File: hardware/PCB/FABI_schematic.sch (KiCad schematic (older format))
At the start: 45 parts, among them J1 Cliff_68125, J10 Conn_01x03_Male, J11 dispaly_connector_91601-304LF, J11_GND1 Conn_01x01_Male, J11_VDD1 Conn_01x01_Male, J11_data1 Conn_01x01_Male, J2 Cliff_68125, J3 Cliff_68125, J4 Cliff_68125, J5 Cliff_68125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

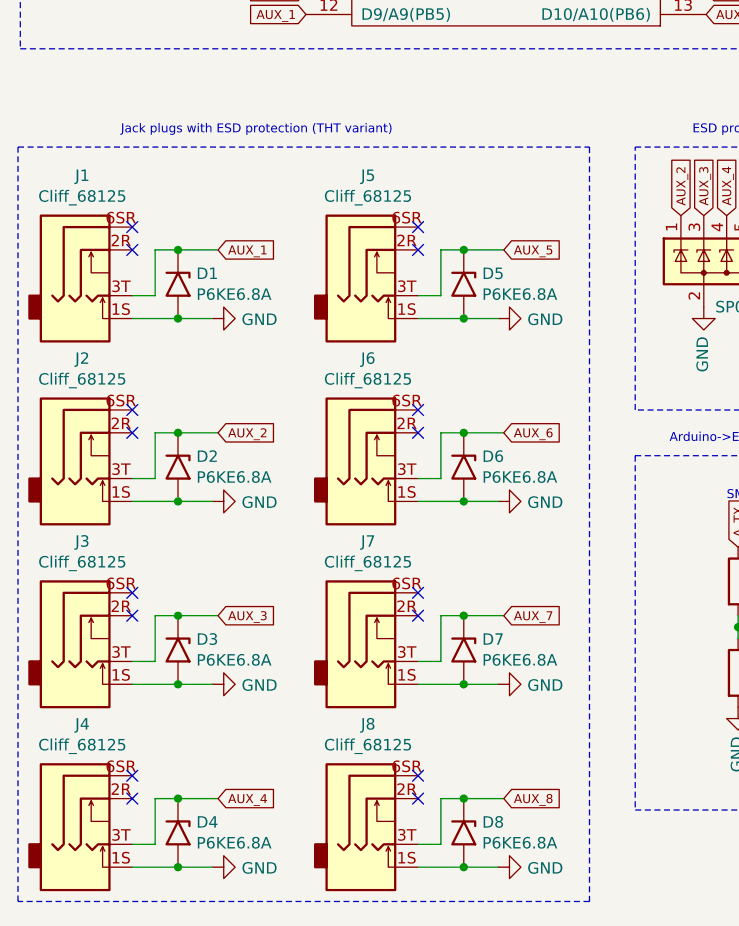
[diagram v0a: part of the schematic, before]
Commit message: JackPlugs in Schematic changed
Signed-off-by: fussthalerandreas <fussthaler.andreas1997@gmail.com>
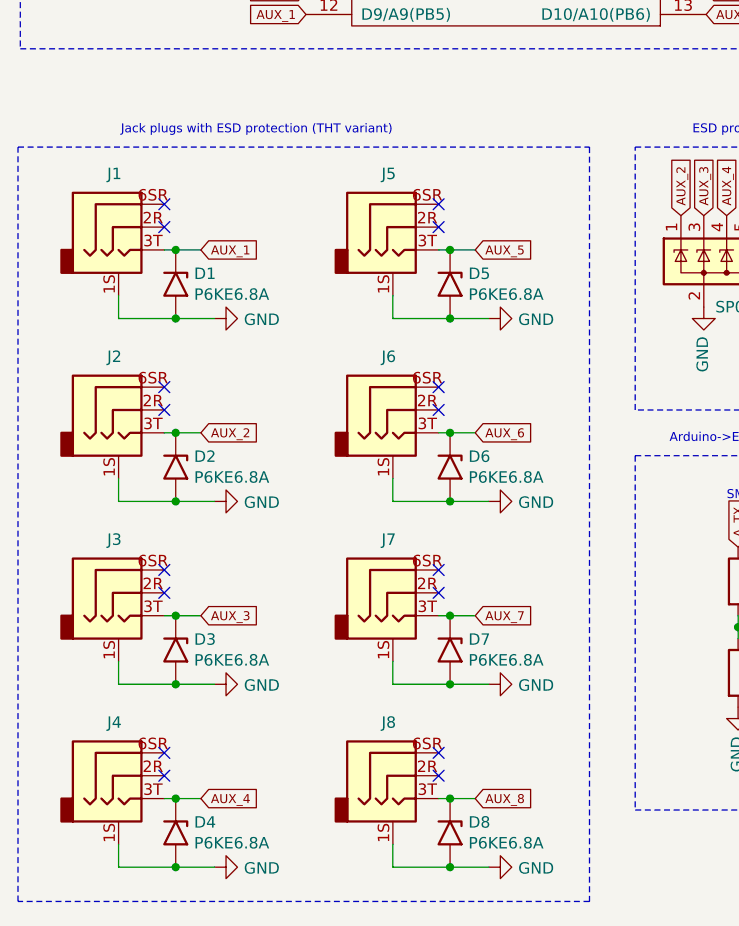
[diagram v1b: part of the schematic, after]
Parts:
- removed J1, J2, J3, J4, J5, J6, J7, J8: Cliff_68125, SamacSys_Parts:FC68125, symbol Connector:Cliff_68125
- added J1, J2, J3, J4, J5, J6, J7, J8: AudioJack3_Ground, SamacSys_Parts:FC68125, symbol FABI_customLib:AudioJack3_Ground
- J11: RS (none) -> https://at.rs-online.com/web/p/leiterplatten-buchsen/673740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
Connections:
- net AUX_1: now also J1.3T
- net AUX_2: now also J2.3T
- net AUX_3: now also J3.3T
- net AUX_4: now also J4.3T
- net AUX_5: now also J5.3T
- net AUX_6: now also J6.3T
- net AUX_7: now also J7.3T
- net AUX_8: now also J8.3T
- net GND: now also J1.1S, J2.1S, J3.1S, J4.1S, J5.1S, J6.1S, J7.1S, J8.1S

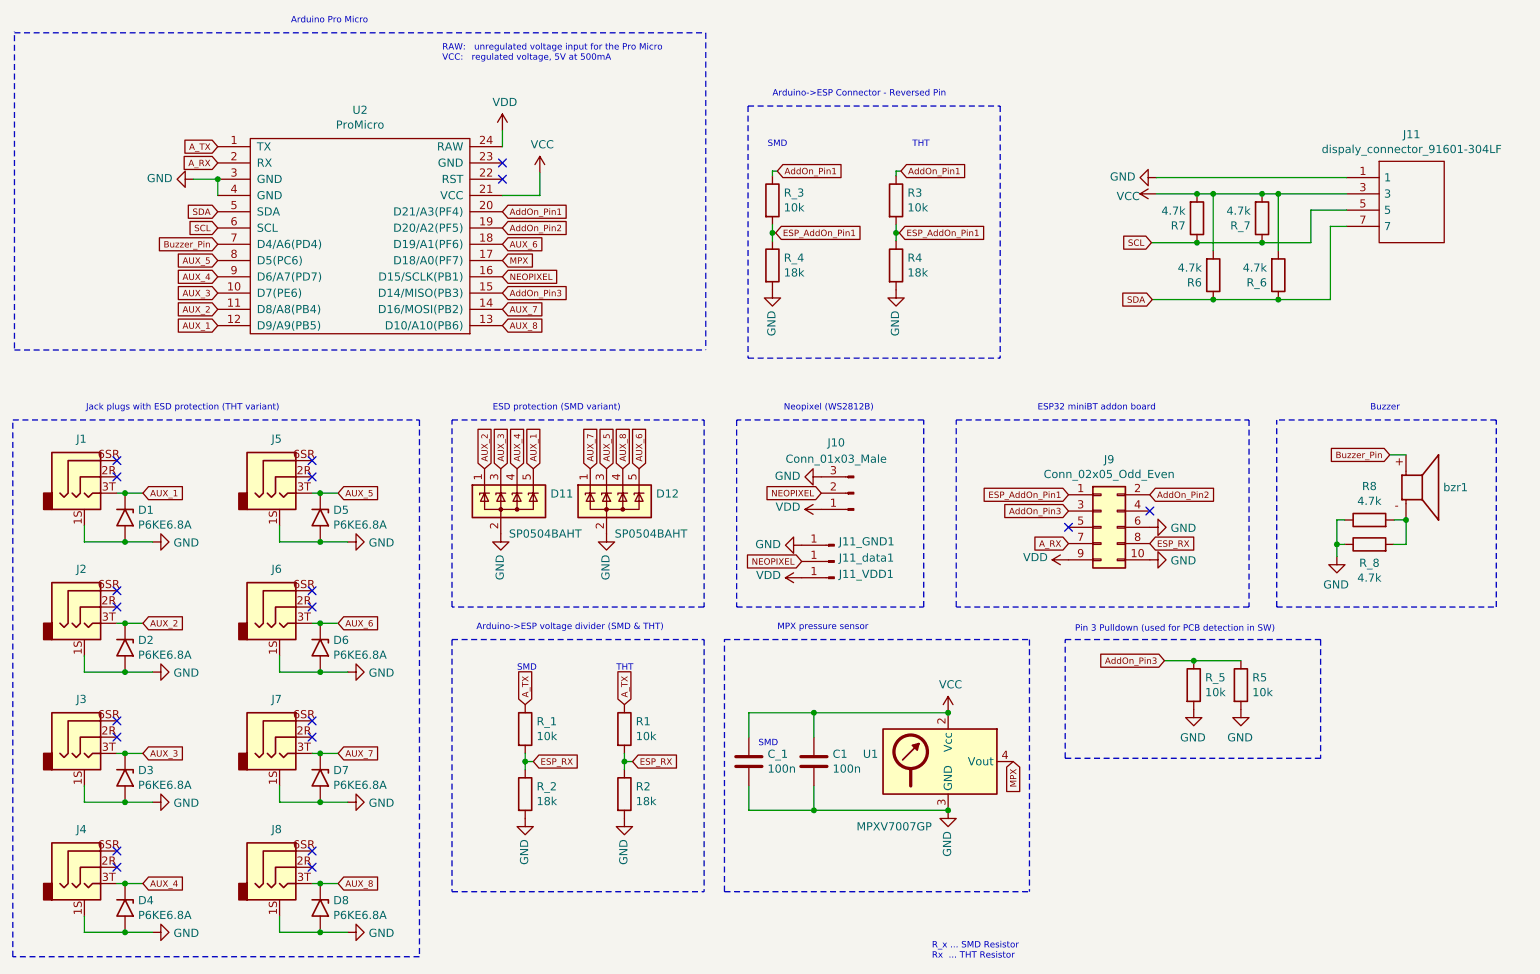
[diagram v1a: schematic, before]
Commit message: ProMicro and most inner components of the PCB shifted to the right by 1.5mm new Buzzer (12mm diameter) Schematics: order infos added & JackPlugs changed
Signed-off-by: fussthalerandreas <fussthaler.andreas1997@gmail.com>
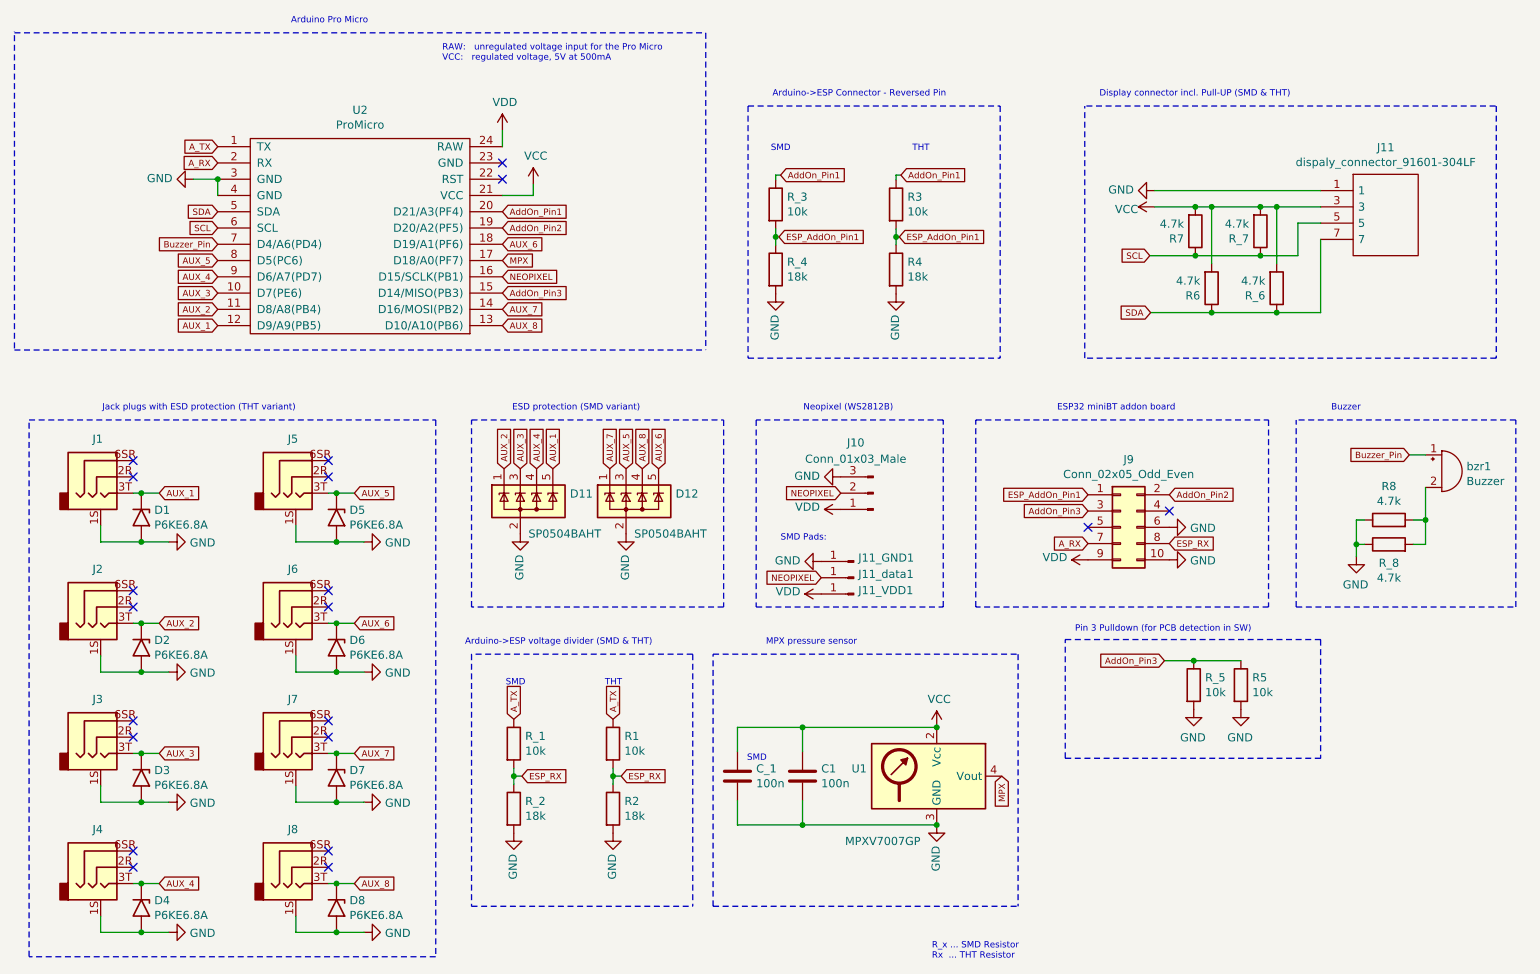
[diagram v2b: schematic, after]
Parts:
- removed bzr1: CMI-9605IC-0380T, CMI-9605IC-0380T:CUI_CMI-9605IC-0380T, symbol CMI-9605IC-0380T:CMI-9605IC-0380T
- added bzr1: Buzzer, Buzzer_Beeper:Buzzer_12x9.5RM7.6, symbol Device:Buzzer
- C1: RS (none) -> https://at.rs-online.com/web/p/keramik-vielschichtkondensat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
- C_1: Farnell (none) -> 1327731; RS (none) -> https://at.rs-online.com/web/p/keramik-vielschichtkondensat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
- D1: RS (none) -> https://at.rs-online.com/web/p/suppressordioden-tvs/1719669/
- D11, D12: RS (none) -> https://at.rs-online.com/web/p/suppressordioden-tvs/7931960/
- D2, D3, D4, D5, D6, D7, D8: RS (none) -> https://at.rs-online.com/web/p/klinken-steckerbuchsen/80516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
- J10: RS (none) -> https://at.rs-online.com/web/p/leiterplatten-header/2518092/; RS-components (none) -> 251-8092
- J9: RS (none) -> https://at.rs-online.com/web/p/leiterplatten-header/2518272/; RS-components (none) -> 251-8272
- U1: Farnell (none) -> https://at.farnell.com/nxp/mpxv7007gp/drucksensor-7-7kpa-so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
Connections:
- net Buzzer_Pin: now also bzr1.1 (-)
- net at R8.2, R_8.2: now also bzr1.2 (+)
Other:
- note added: "Display connector incl. Pull-UP (SMD & THT)"
- note added: "Pin 3 Pulldown (for PCB detection in SW)"
- note added: "SMD Pads:"
- note removed: "Pin 3 Pulldown (used for PCB detection in SW)"
- moved on the sheet: C1, C_1, D1, D11, D12, D2, D3, D4, D5, D6, D7, D8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

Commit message: small final adjustment (Silk placements) before production of first prototype
Signed-off-by: fussthalerandreas <fussthaler.andreas1997@gmail.com>
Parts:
- C_1: RS https://at.rs-online.com/web/p/keramik-vielschichtkondensatoren/1243314/ -> https://at.rs-online.com/web/p/keramik-vielschichtkondensatoren/4646688/
- R1, R2, R3, R4, R5, R6, R7, R8: RS (none) -> https://at.rs-online.com/web/p/widerstande-durchsteckmontag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
- R_1, R_3, R_5: RS (none) -> https://at.rs-online.com/web/p/smd-widerstande/8123375/
- R_2, R_4: RS (none) -> https://at.rs-online.com/web/p/smd-widerstande/9059694/
- R_6, R_7, R_8: RS (none) -> https://at.rs-online.com/web/p/smd-widerstande/9059679/
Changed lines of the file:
@@
 F 2 "Resistor_THT:R_Axial_DIN0204_L3.6mm_D1.6mm_P7.62mm_Horizontal" V 8990 4965 50  0001 C CNN
 F 3 "~" H 9060 4965 50  0001 C CNN
+F 4 "https://at.rs-online.com/web/p/widerstande-durchsteckmontage/1650319/" V 9060 4965 50  0001 C CNN "RS"
 	1    9060 4965
 	0    -1   -1   0
@@
 F 2 "Resistor_SMD:R_0805_2012Metric_Pad1.20x1.40mm_HandSolder" V 8990 5115 50  0001 C CNN
 F 3 "~" H 9060 5115 50  0001 C CNN
+F 4 "https://at.rs-online.com/web/p/smd-widerstande/9059679/" V 9060 5115 50  0001 C CNN "RS"
 	1    9060 5115
 	0    -1   -1   0
@@
 F 2 "Resistor_THT:R_Axial_DIN0204_L3.6mm_D1.6mm_P7.62mm_Horizontal" V 8080 5980 50  0001 C CNN
 F 3 "~" H 8150 5980 50  0001 C CNN
+F 4 "https://at.rs-online.com/web/p/widerstande-durchsteckmontage/1650369/" H 8150 5980 50  0001 C CNN "RS"
 	1    8150 5980
 	1    0    0    -1
@@
 F 2 "Resistor_SMD:R_0805_2012Metric_Pad1.20x1.40mm_HandSolder" V 7790 5980 50  0001 C CNN
 F 3 "~" H 7860 5980 50  0001 C CNN
+F 4 "https://at.rs-online.com/web/p/smd-widerstande/8123375/" H 7860 5980 50  0001 C CNN "RS"
 	1    7860 5980
 	1    0    0    -1
@@
 F 2 "Resistor_SMD:R_0805_2012Metric_Pad1.20x1.40mm_HandSolder" V 8300 3540 50  0001 C CNN
 F 3 "~" H 8370 3540 50  0001 C CNN
+F 4 "https://at.rs-online.com/web/p/smd-widerstande/9059679/" H 8370 3540 50  0001 C CNN "RS"
 	1    8370 3540
 	1    0    0    1
@@
 F 2 "Resistor_SMD:R_0805_2012Metric_Pad1.20x1.40mm_HandSolder" V 8200 3190 50  0001 C CNN
 F 3 "~" H 8270 3190 50  0001 C CNN
+F 4 "https://at.rs-online.com/web/p/smd-widerstande/9059679/" H 8270 3190 50  0001 C CNN "RS"
 	1    8270 3190
 	1    0    0    1
@@
 F 2 "Resistor_THT:R_Axial_DIN0204_L3.6mm_D1.6mm_P7.62mm_Horizontal" V 7800 3190 50  0001 C CNN
 F 3 "~" H 7870 3190 50  0001 C CNN
+F 4 "https://at.rs-online.com/web/p/widerstande-durchsteckmontage/1650319/" H 7870 3190 50  0001 C CNN "RS"
 	1    7870 3190
 	1    0    0    1
@@
 F 2 "Resistor_THT:R_Axial_DIN0204_L3.6mm_D1.6mm_P7.62mm_Horizontal" V 7900 3540 50  0001 C CNN
 F 3 "~" H 7970 3540 50  0001 C CNN
+F 4 "https://at.rs-online.com/web/p/widerstande-durchsteckmontage/1650319/" H 7970 3540 50  0001 C CNN "RS"
 	1    7970 3540
 	1    0    0    1
@@
 F 2 "Resistor_SMD:R_0805_2012Metric_Pad1.20x1.40mm_HandSolder" V 5220 3025 50  0001 C CNN
 F 3 "~" H 5290 3025 50  0001 C CNN
+F 4 "https://at.rs-online.com/web/p/smd-widerstande/8123375/" H 5290 3025 50  0001 C CNN "RS"
 	1    5290 3025
 	1    0    0    -1
@@
 F 2 "Resistor_SMD:R_0805_2012Metric_Pad1.20x1.40mm_HandSolder" V 5220 3425 50  0001 C CNN
 F 3 "~" H 5290 3425 50  0001 C CNN
+F 4 "https://at.rs-online.com/web/p/smd-widerstande/9059694/" H 5290 3425 50  0001 C CNN "RS"
 	1    5290 3425
 	1    0    0    -1
@@
 F 2 "Resistor_THT:R_Axial_DIN0204_L3.6mm_D1.6mm_P7.62mm_Horizontal" V 5960 3425 50  0001 C CNN
 F 3 "~" H 6030 3425 50  0001 C CNN
+F 4 "https://at.rs-online.com/web/p/widerstande-durchsteckmontage/1997554/" H 6030 3425 50  0001 C CNN "RS"
 	1    6030 3425
 	1    0    0    -1
@@
 F 2 "Resistor_THT:R_Axial_DIN0204_L3.6mm_D1.6mm_P7.62mm_Horizontal" V 5960 3025 50  0001 C CNN
 F 3 "~" H 6030 3025 50  0001 C CNN
+F 4 "https://at.rs-online.com/web/p/widerstande-durchsteckmontage/1650369/" H 6030 3025 50  0001 C CNN "RS"
 	1    6030 3025
 	1    0    0    -1
@@
 F 2 "Resistor_THT:R_Axial_DIN0204_L3.6mm_D1.6mm_P7.62mm_Horizontal" V 4220 6340 50  0001 C CNN
 F 3 "~" H 4290 6340 50  0001 C CNN
+F 4 "https://at.rs-online.com/web/p/widerstande-durchsteckmontage/1650369/" H 4290 6340 50  0001 C CNN "RS"
 	1    4290 6340
 	1    0    0    -1
@@
 F 3 "~" H 5055 6540 50  0001 C CNN
 F 4 "1327731" H 5055 6540 50  0001 C CNN "Farnell"
-F 5 "https://at.rs-online.com/web/p/keramik-vielschichtkondensatoren/1243314/" H 5055 6540 50  0001 C CNN "RS"
+F 5 "https://at.rs-online.com/web/p/keramik-vielschichtkondensatoren/4646688/" H 5055 6540 50  0001 C CNN "RS"
 	1    5055 6540
 	1    0    0    -1
@@
 F 2 "Resistor_SMD:R_0805_2012Metric_Pad1.20x1.40mm_HandSolder" V 3610 6340 50  0001 C CNN
 F 3 "~" H 3680 6340 50  0001 C CNN
+F 4 "https://at.rs-online.com/web/p/smd-widerstande/8123375/" H 3680 6340 50  0001 C CNN "RS"
 	1    3680 6340
 	1    0    0    -1
@@
 F 2 "Resistor_SMD:R_0805_2012Metric_Pad1.20x1.40mm_HandSolder" V 3610 6740 50  0001 C CNN
 F 3 "~" H 3680 6740 50  0001 C CNN
+F 4 "https://at.rs-online.com/web/p/smd-widerstande/9059694/" H 3680 6740 50  0001 C CNN "RS"
 	1    3680 6740
 	1    0    0    -1
@@
 F 2 "Resistor_THT:R_Axial_DIN0204_L3.6mm_D1.6mm_P7.62mm_Horizontal" V 4220 6740 50  0001 C CNN
 F 3 "~" H 4290 6740 50  0001 C CNN
+F 4 "https://at.rs-online.com/web/p/widerstande-durchsteckmontage/1997554/" H 4290 6740 50  0001 C CNN "RS"
 	1    4290 6740
 	1    0    0    -1

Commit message: BOM-Export and elemnt property adjustments
Signed-off-by: fussthalerandreas <fussthaler.andreas1997@gmail.com>
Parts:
- C_1: Farnell 1327731 -> (none); Farnell-Nr (none) -> 1327731
- D1: Farnell 1703028 -> (none); Farnell-Nr (none) -> 1703028
- D2, D3, D4, D5, D6, D7, D8: Farnell 1703028 -> (none); Farnell-Nr (none) -> 1703028; RS https://at.rs-online.com/web/p/klinken-steckerbuchsen/80516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 -> https://at.rs-online.com/web/p/suppressordioden-tvs/1719669/
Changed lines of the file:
@@
 F 2 "Diode_THT:D_DO-201AE_P12.70mm_Horizontal" H 1390 4750 50  0001 C CNN
 F 3 "https://www.vishay.com/docs/88301/15ke.pdf" H 1340 4950 50  0001 C CNN
-F 4 "1703028" V 1390 4950 50  0001 C CNN "Farnell"
+F 4 "1703028" V 1390 4950 50  0001 C CNN "Farnell-Nr"
 F 5 "171-9669" V 1390 4950 50  0001 C CNN "RS-components"
 F 6 "https://at.rs-online.com/web/p/suppressordioden-tvs/1719669/" V 1390 4950 50  0001 C CNN "RS"
@@
 F 2 "Diode_THT:D_DO-201AE_P12.70mm_Horizontal" H 1390 5550 50  0001 C CNN
 F 3 "https://www.vishay.com/docs/88301/15ke.pdf" H 1340 5750 50  0001 C CNN
-F 4 "1703028" V 1390 5750 50  0001 C CNN "Farnell"
+F 4 "1703028" V 1390 5750 50  0001 C CNN "Farnell-Nr"
 F 5 "171-9669" V 1390 5750 50  0001 C CNN "RS-components"
-F 6 "https://at.rs-online.com/web/p/klinken-steckerbuchsen/8051655/" V 1390 5750 50  0001 C CNN "RS"
+F 6 "https://at.rs-online.com/web/p/suppressordioden-tvs/1719669/" V 1390 5750 50  0001 C CNN "RS"
 	1    1390 5750
 	0    1    1    0
@@
 F 2 "Diode_THT:D_DO-201AE_P12.70mm_Horizontal" H 1390 6350 50  0001 C CNN
 F 3 "https://www.vishay.com/docs/88301/15ke.pdf" H 1340 6550 50  0001 C CNN
-F 4 "1703028" V 1390 6550 50  0001 C CNN "Farnell"
+F 4 "1703028" V 1390 6550 50  0001 C CNN "Farnell-Nr"
 F 5 "171-9669" V 1390 6550 50  0001 C CNN "RS-components"
-F 6 "https://at.rs-online.com/web/p/klinken-steckerbuchsen/8051655/" V 1390 6550 50  0001 C CNN "RS"
+F 6 "https://at.rs-online.com/web/p/suppressordioden-tvs/1719669/" V 1390 6550 50  0001 C CNN "RS"
 	1    1390 6550
 	0    1    1    0
@@
 F 2 "Diode_THT:D_DO-201AE_P12.70mm_Horizontal" H 1390 7150 50  0001 C CNN
 F 3 "https://www.vishay.com/docs/88301/15ke.pdf" H 1340 7350 50  0001 C CNN
-F 4 "1703028" V 1390 7350 50  0001 C CNN "Farnell"
+F 4 "1703028" V 1390 7350 50  0001 C CNN "Farnell-Nr"
 F 5 "171-9669" V 1390 7350 50  0001 C CNN "RS-components"
-F 6 "https://at.rs-online.com/web/p/klinken-steckerbuchsen/8051655/" V 1390 7350 50  0001 C CNN "RS"
+F 6 "https://at.rs-online.com/web/p/suppressordioden-tvs/1719669/" V 1390 7350 50  0001 C CNN "RS"
 	1    1390 7350
 	0    1    1    0
@@
 F 2 "Diode_THT:D_DO-201AE_P12.70mm_Horizontal" H 2590 4750 50  0001 C CNN
 F 3 "https://www.vishay.com/docs/88301/15ke.pdf" H 2540 4950 50  0001 C CNN
-F 4 "1703028" V 2590 4950 50  0001 C CNN "Farnell"
+F 4 "1703028" V 2590 4950 50  0001 C CNN "Farnell-Nr"
 F 5 "171-9669" V 2590 4950 50  0001 C CNN "RS-components"
-F 6 "https://at.rs-online.com/web/p/klinken-steckerbuchsen/8051655/" V 2590 4950 50  0001 C CNN "RS"
+F 6 "https://at.rs-online.com/web/p/suppressordioden-tvs/1719669/" V 2590 4950 50  0001 C CNN "RS"
 	1    2590 4950
 	0    1    1    0
@@
 F 2 "Diode_THT:D_DO-201AE_P12.70mm_Horizontal" H 2590 5550 50  0001 C CNN
 F 3 "https://www.vishay.com/docs/88301/15ke.pdf" H 2540 5750 50  0001 C CNN
-F 4 "1703028" V 2590 5750 50  0001 C CNN "Farnell"
+F 4 "1703028" V 2590 5750 50  0001 C CNN "Farnell-Nr"
 F 5 "171-9669" V 2590 5750 50  0001 C CNN "RS-components"
-F 6 "https://at.rs-online.com/web/p/klinken-steckerbuchsen/8051655/" V 2590 5750 50  0001 C CNN "RS"
+F 6 "https://at.rs-online.com/web/p/suppressordioden-tvs/1719669/" V 2590 5750 50  0001 C CNN "RS"
 	1    2590 5750
 	0    1    1    0
@@
 F 2 "Diode_THT:D_DO-201AE_P12.70mm_Horizontal" H 2590 6350 50  0001 C CNN
 F 3 "https://www.vishay.com/docs/88301/15ke.pdf" H 2540 6550 50  0001 C CNN
-F 4 "1703028" V 2590 6550 50  0001 C CNN "Farnell"
+F 4 "1703028" V 2590 6550 50  0001 C CNN "Farnell-Nr"
 F 5 "171-9669" V 2590 6550 50  0001 C CNN "RS-components"
-F 6 "https://at.rs-online.com/web/p/klinken-steckerbuchsen/8051655/" V 2590 6550 50  0001 C CNN "RS"
+F 6 "https://at.rs-online.com/web/p/suppressordioden-tvs/1719669/" V 2590 6550 50  0001 C CNN "RS"
 	1    2590 6550
 	0    1    1    0
@@
 F 2 "Diode_THT:D_DO-201AE_P12.70mm_Horizontal" H 2590 7150 50  0001 C CNN
 F 3 "https://www.vishay.com/docs/88301/15ke.pdf" H 2540 7350 50  0001 C CNN
-F 4 "1703028" V 2590 7350 50  0001 C CNN "Farnell"
+F 4 "1703028" V 2590 7350 50  0001 C CNN "Farnell-Nr"
 F 5 "171-9669" V 2590 7350 50  0001 C CNN "RS-components"
-F 6 "https://at.rs-online.com/web/p/klinken-steckerbuchsen/8051655/" V 2590 7350 50  0001 C CNN "RS"
+F 6 "https://at.rs-online.com/web/p/suppressordioden-tvs/1719669/" V 2590 7350 50  0001 C CNN "RS"
 	1    2590 7350
 	0    1    1    0
@@
 F 2 "Capacitor_SMD:C_0805_2012Metric_Pad1.18x1.45mm_HandSolder" H 5093 6390 50  0001 C CNN
 F 3 "~" H 5055 6540 50  0001 C CNN
-F 4 "1327731" H 5055 6540 50  0001 C CNN "Farnell"
+F 4 "1327731" H 5055 6540 50  0001 C CNN "Farnell-Nr"
 F 5 "https://at.rs-online.com/web/p/keramik-vielschichtkondensatoren/4646688/" H 5055 6540 50  0001 C CNN "RS"
 	1    5055 6540
